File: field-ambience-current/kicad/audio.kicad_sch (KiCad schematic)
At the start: 24 parts, among them J6 Speaker L (PUI AS04008PS, 4R 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, J7 Speaker R (PUI AS04008PS, 4R 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, U3 PCM5102A I²S DAC (TSSOP-20), U4 PAM8403H Class-D Stereo Amp (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

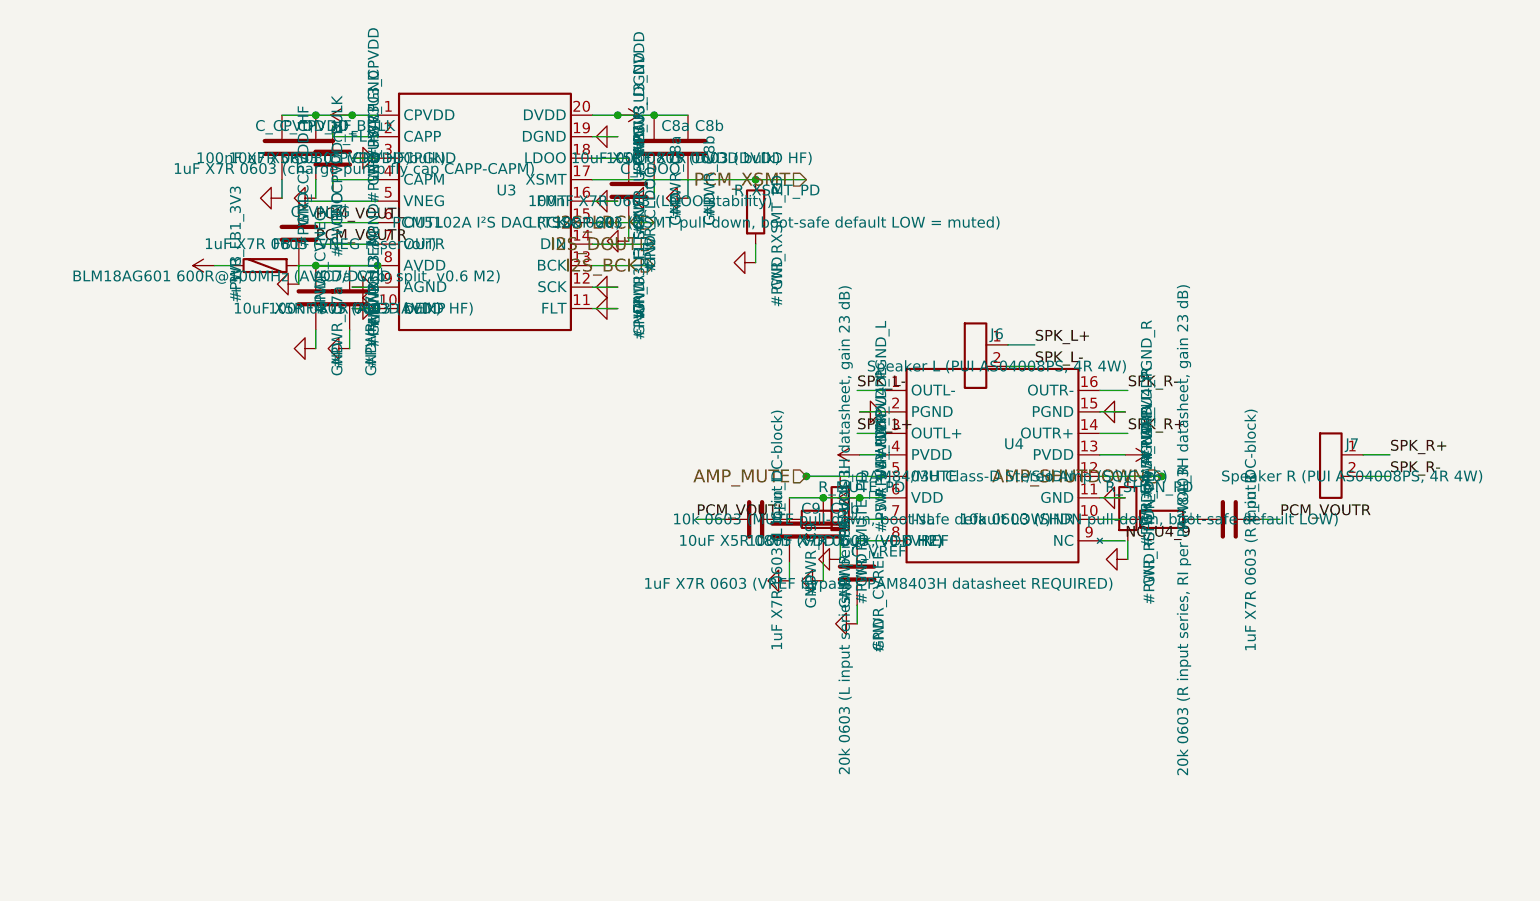
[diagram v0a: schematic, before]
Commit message: v0.6.3-r6: Stabilization pass — PVDD decoupling, startup sequence, SPEC consolidation
No new features. Pure stabilization per senior-engineer review.

=== HIGH fixes ===

1. PAM8403H PVDD decoupling (pins 4, 13) — was missing
   Datasheet (PAM8403H.PDF "Application Information") requires:
   "1.0µF ceramic close to VDD" (HF) + "20µF or greater" (bulk).
   Previous: only C9 10µF + C9b 100nF at VDD (pin 6). PVDD pins 4 (L)
   and 13 (R) had no local decoupling → Class-D 250kHz switching
   transients would modulate PVDD → distortion at volume + EMI.
   Fix:
   - Left (VDD pin6 + PVDD-L pin4): C9 10µF→22µF (C45783), C9b 100nF→1µF
   - Right (PVDD-R pin13): NEW C_PVDDR 22µF + C_PVDDR_HF 1µF local
   Note: corrected my own earlier review — PVDD is pins 4+13 only,
   NOT 4/10/13 (pin 10 is INR input, not power).

2. PAM8403 startup sequence — was in wrong order in SPEC
   SPEC §8 had: /MUTE=HIGH first, then /SHDN=HIGH 100ms later.
   Both are active-LOW. Un-muting before chip wakeup means audio
   passes the instant /SHDN goes HIGH → pop.
   Fix: /SHDN=HIGH first (chip wakes, references settle, output still
   muted via /MUTE=LOW), then /MUTE=HIGH 50ms later. Shutdown reverses.
   Corrected in SPEC §5 AND §8 body (not just errata).

=== SPEC consolidation (single source of truth) ===

- Moved entire Errata-Historie (v0.6.1 → v0.6.3-r5, 327 lines) out of
  SPEC body into new CHANGELOG.md
- SPEC header rewritten: clean rev marker, status "SCHEMATIC IN REVIEW"
- SPEC body now describes ONLY the current state, no errata/old-value
  contradictions
- §3 decoupling table updated: C9 22µF, C9b 1µF, + C_PVDDR/C_PVDDR_HF,
  + C_VREF rows added
- §5 + §8: startup sequence corrected, active-low convention documented

=== Cross-domain fix: AMP signal naming ===

Renamed AMP_SHUTDOWN → AMP_nSHDN, AMP_MUTE → AMP_nMUTE throughout the
generator (17 occurrences). Both PAM8403H /SHDN and /MUTE are active-LOW;
old names implied active-high and were a firmware-bug magnet. SPEC §5
already used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
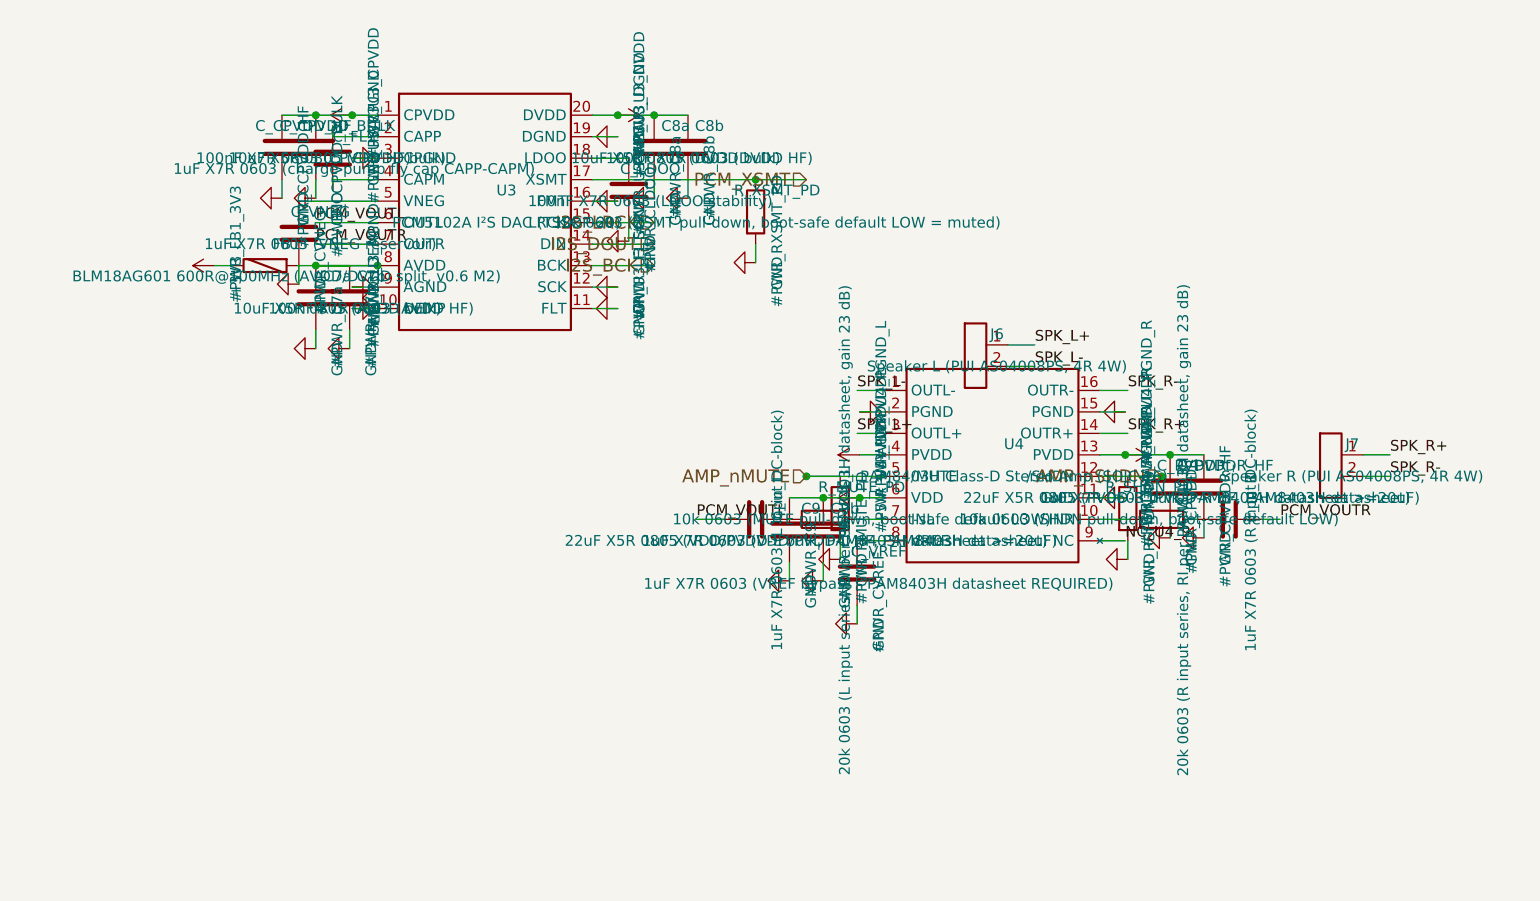
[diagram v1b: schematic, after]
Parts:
- added C_PVDDR: 22uF X5R 0805 (PVDD-R bulk, PAM8403H datasheet >=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, Capacitor_SMD:C_0805_2012Metric, symbol Device:C
- added C_PVDDR_HF: 1uF X7R 0603 (PVDD-R HF, PAM8403H datasheet), Capacitor_SMD:C_0603_1608Metric, symbol Device:C
- C9: value 10uF X5R 0805 (VDD bulk, v0.6 H2) -> 22uF X5R 0805 (VDD/PVDD-L bulk, PAM8403H datasheet >=20uF); LCSC C15850 -> C45783; MPN CL21A106KOQNNNE -> CL21A226MAQNNNE
- C9b: value 100nF X7R 0603 (VDD HF) -> 1uF X7R 0603 (VDD/PVDD-L HF, PAM8403H datasheet); LCSC C14663 -> C15849; MPN CC0603KRX7R9BB104 -> CC0603KRX7R7BB105
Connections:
- net +5V: now also C_PVDDR.1, C_PVDDR_HF.1
- net GND: now also C_PVDDR.2, C_PVDDR_HF.2
- net AMP_MUTE renamed AMP_nMUTE
- net AMP_SHUTDOWN renamed AMP_nSHDN
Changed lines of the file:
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@@
       (property "Reference" "C9b" (at 142.54 135.08 0)
         (effects (font (size 1.27 1.27))))
-      (property "Value" "100nF X7R 0603 (VDD HF)" (at 142.54 138.89000000000001 0)
+      (property "Value" "1uF X7R 0603 (VDD/PVDD-L HF, PAM8403H datasheet)" (at 142.54 138.89000000000001 0)
         (effects (font (size 1.27 1.27))))
       (property "Footprint" "Capacitor_SMD:C_0603_1608Metric" (at 140 137.62 0)
@@
       (property "Datasheet" "~" (at 140 137.62 0)
         (effects (font (size 1.27 1.27)) hide))
-      (property "MPN" "CC0603KRX7R9BB104" (at 142.54 141.43 0)
-        (effects (font (size 1.27 1.27)) hide))
-      (property "LCSC" "C14663" (at 142.54 142.70000000000002 0)
+      (property "MPN" "CC0603KRX7R7BB105" (at 142.54 141.43 0)
+        (effects (font (size 1.27 1.27)) hide))
+      (property "LCSC" "C15849" (at 142.54 142.70000000000002 0)
         (effects (font (size 1.27 1.27)) hide))
     (instances
@@
       (property "Reference" "C9" (at 138.54 135.08 0)
         (effects (font (size 1.27 1.27))))
-      (property "Value" "10uF X5R 0805 (VDD bulk, v0.6 H2)" (at 138.54 138.89000000000001 0)
+      (property "Value" "22uF X5R 0805 (VDD/PVDD-L bulk, PAM8403H datasheet >=20uF)" (at 138.54 138.89000000000001 0)
         (effects (font (size 1.27 1.27))))
       (property "Footprint" "Capacitor_SMD:C_0805_2012Metric" (at 136 137.62 0)
@@
       (property "Datasheet" "~" (at 136 137.62 0)
         (effects (font (size 1.27 1.27)) hide))
-      (property "MPN" "CL21A106KOQNNNE" (at 138.54 141.43 0)
-        (effects (font (size 1.27 1.27)) hide))
-      (property "LCSC" "C15850" (at 138.54 142.70000000000002 0)
+      (property "MPN" "CL21A226MAQNNNE" (at 138.54 141.43 0)
+        (effects (font (size 1.27 1.27)) hide))
+      (property "LCSC" "C45783" (at 138.54 142.70000000000002 0)
         (effects (font (size 1.27 1.27)) hide))
     (instances
@@
       (project "field_ambience"
         (path "/66fcdc89-be06-4d61-a855-abf9641d963c" (reference "#PWR_U4_PVDDR") (unit 1)))))
+  (symbol (lib_id "Device:C") (at 181 132.54 0) (unit 1)
+    (in_bom yes) (on_board yes) (dnp no)
+      (property "Reference" "C_PVDDR" (at 183.54 130.0 0)
+        (effects (font (size 1.27 1.27))))
+      (property "Value" "22uF X5R 0805 (PVDD-R bulk, PAM8403H datasheet >=20uF)" (at 183.54 133.81 0)
+        (effects (font (size 1.27 1.27))))
+      (property "Footprint" "Capacitor_SMD:C_0805_2012Metric" (at 181 132.54 0)
+        (effects (font (size 1.27 1.27)) hide))
+      (property "Datasheet" "~" (at 181 132.54 0)
+        (effects (font (size 1.27 1.27)) hide))
+      (property "MPN" "CL21A226MAQNNNE" (at 183.54 136.35 0)
+        (effects (font (size 1.27 1.27)) hide))
+      (property "LCSC" "C45783" (at 183.54 137.62 0)
+        (effects (font (size 1.27 1.27)) hide))
+    (instances
+      (project "field_ambience"
+        (path "/66fcdc89-be06-4d61-a855-abf9641d963c" (reference "C_PVDDR") (unit 1)))))
+  (symbol (lib_id "Power:GND") (at 181 138.54 270) (unit 1)
+    (in_bom yes) (on_board yes) (dnp no)
+      (property "Reference" "#PWR_CPVDDR" (at 183.54 136.0 0)
+        (effects (font (size 1.27 1.27))))
+      (property "Value" "GND" (at 183.54 139.81 0)
+        (effects (font (size 1.27 1.27))))
+      (property "Footprint" "" (at 181 138.54 0)
+        (effects (font (size 1.27 1.27)) hide))
+      (property "Datasheet" "~" (at 181 138.54 0)
+        (effects (font (size 1.27 1.27)) hide))
+    (instances
+      (project "field_ambience"
+        (path "/66fcdc89-be06-4d61-a855-abf9641d963c" (reference "#PWR_CPVDDR") (unit 1)))))
+  (symbol (lib_id "Device:C") (at 185 132.54 0) (unit 1)
+    (in_bom yes) (on_board yes) (dnp no)
+      (property "Reference" "C_PVDDR_HF" (at 187.54 130.0 0)
+        (effects (font (size 1.27 1.27))))
+      (property "Value" "1uF X7R 0603 (PVDD-R HF, PAM8403H datasheet)" (at 187.54 133.81 0)
+        (effects (font (size 1.27 1.27))))
+      (property "Footprint" "Capacitor_SMD:C_0603_1608Metric" (at 185 132.54 0)
+        (effects (font (size 1.27 1.27)) hide))
+      (property "Datasheet" "~" (at 185 132.54 0)
+        (effects (font (size 1.27 1.27)) hide))
+      (property "MPN" "CC0603KRX7R7BB105" (at 187.54 136.35 0)
+        (effects (font (size 1.27 1.27)) hide))
+      (property "LCSC" "C15849" (at 187.54 137.62 0)
+        (effects (font (size 1.27 1.27)) hide))
+    (instances
+      (project "field_ambience"
+        (path "/66fcdc89-be06-4d61-a855-abf9641d963c" (reference "C_PVDDR_HF") (unit 1)))))
+  (symbol (lib_id "Power:GND") (at 185 138.54 270) (unit 1)
+    (in_bom yes) (on_board yes) (dnp no)
+      (property "Reference" "#PWR_CPVDDR_HF" (at 187.54 136.0 0)
+        (effects (font (size 1.27 1.27))))
+      (property "Value" "GND" (at 187.54 139.81 0)
+        (effects (font (size 1.27 1.27))))
+      (property "Footprint" "" (at 185 138.54 0)
+        (effects (font (size 1.27 1.27)) hide))
+      (property "Datasheet" "~" (at 185 138.54 0)
+        (effects (font (size 1.27 1.27)) hide))
+    (instances
+      (project "field_ambience"
+        (path "/66fcdc89-be06-4d61-a855-abf9641d963c" (reference "#PWR_CPVDDR_HF") (unit 1)))))
   (symbol (lib_id "Power:GND") (at 175.7 123.65 270) (unit 1)
     (in_bom yes) (on_board yes) (dnp no)
@@
     (stroke (width 0) (type default))
 )
+  (wire (pts (xy 181 128.73) (xy 175.7 128.73))
+    (stroke (width 0) (type default))
+)
+  (wire (pts (xy 181 136.35) (xy 181 138.54))
+    (stroke (width 0) (type default))
+)
+  (wire (pts (xy 185 128.73) (xy 181 128.73))
+    (stroke (width 0) (type default))
+)
+  (wire (pts (xy 185 136.35) (xy 185 138.54))
+    (stroke (width 0) (type default))
+)
   (wire (pts (xy 172.7 126.19) (xy 176 126.19))
     (stroke (width 0) (type default))
@@
 )
   (junction (at 180 131.27) (diameter 0) (color 0 0 0 0)
+)
+  (junction (at 175.7 128.73) (diameter 0) (color 0 0 0 0)
+)
+  (junction (at 181 128.73) (diameter 0) (color 0 0 0 0)
 )
   (label "PCM_VOUTL" (at 80 101.27 0) (fields_autoplaced)
@@
     (effects (font (size 1.524 1.524)) (justify right))
 )
-  (hierarchical_label "AMP_MUTE" (shape input) (at 138 131.27 0)
+  (hierarchical_label "AMP_nMUTE" (shape input) (at 138 131.27 0)
     (effects (font (size 1.524 1.524)) (justify right))
 )
-  (hierarchical_label "AMP_SHUTDOWN" (shape input) (at 180 131.27 180)
+  (hierarchical_label "AMP_nSHDN" (shape input) (at 180 131.27 180)
     (effects (font (size 1.524 1.524)) (justify right))
 )
